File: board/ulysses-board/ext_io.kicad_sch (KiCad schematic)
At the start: 31 parts, among them J10 CAN_2, J6 AIN, J7 CAN_1, J8 DIO_1, J9 DIO_0, U12 25LCxxx, U13 MCP3204, U14 MCP2515-I/P, U15 MCP2562-E-P, U16 MCP2515-I/P, U17 MCP23S17, U18 MCP2562-E-P, Y1 16MHz, Y2 16MHz

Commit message: Make some minor fixes.
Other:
- note added: "Analog input"
- note removed: "ADC input"
- moved on the sheet: C19, U12

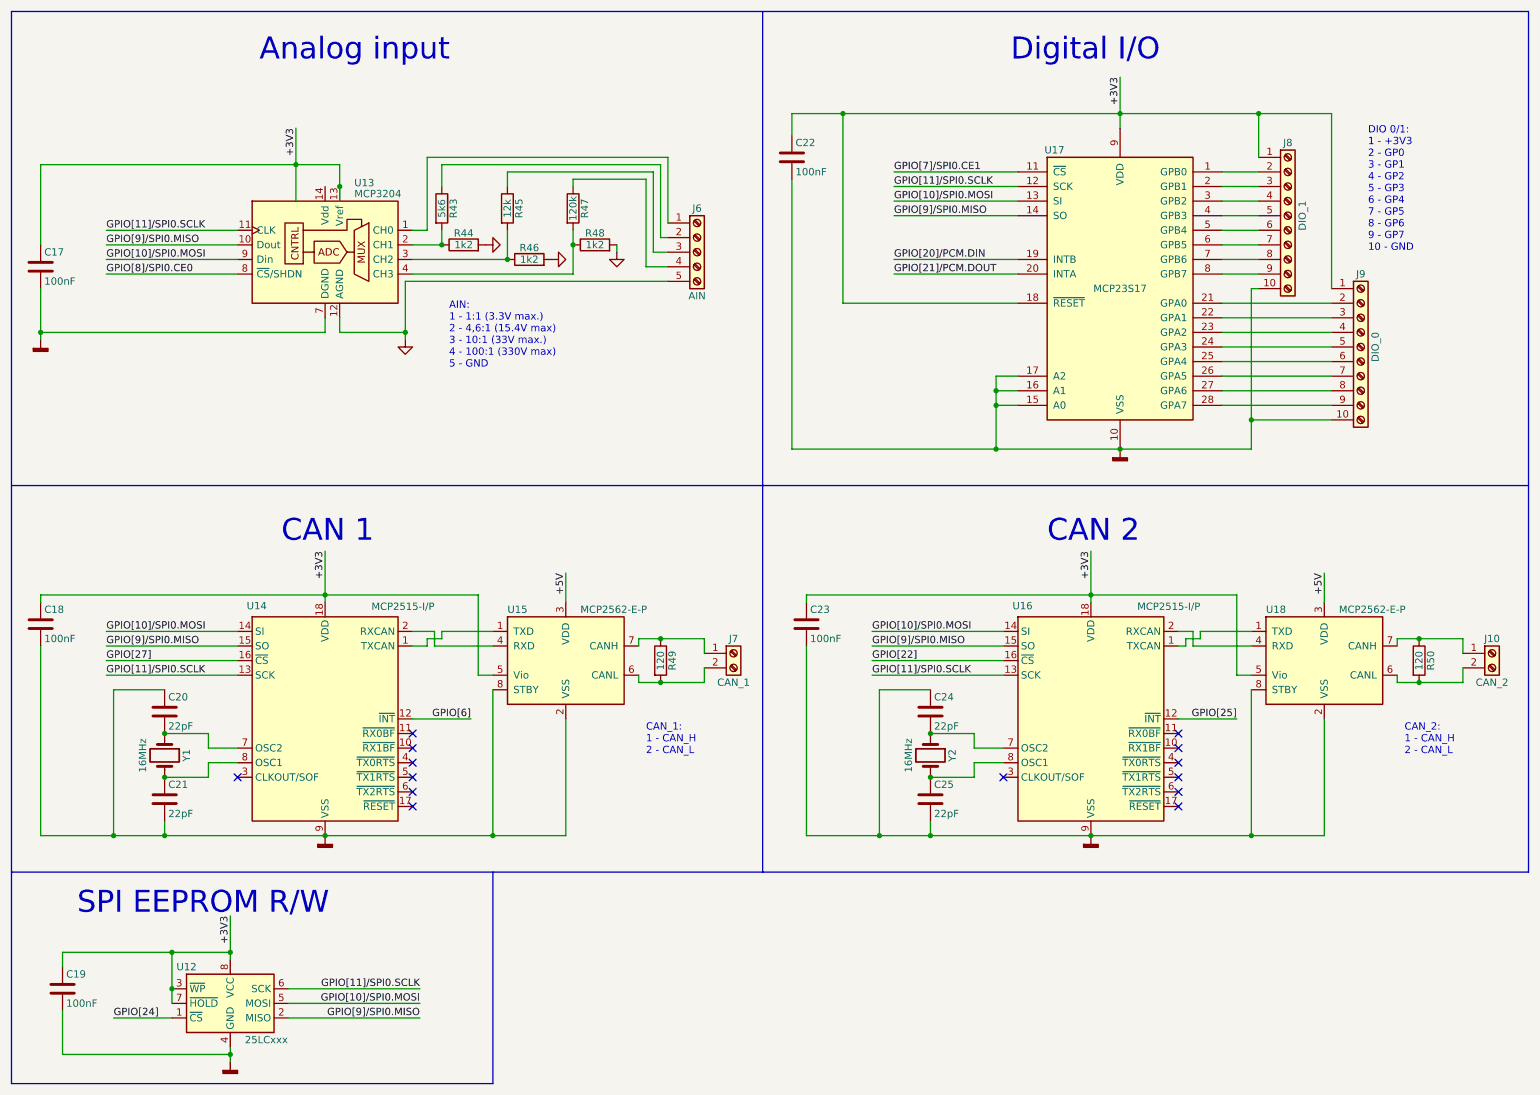
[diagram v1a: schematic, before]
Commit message: Add a real-time clock.
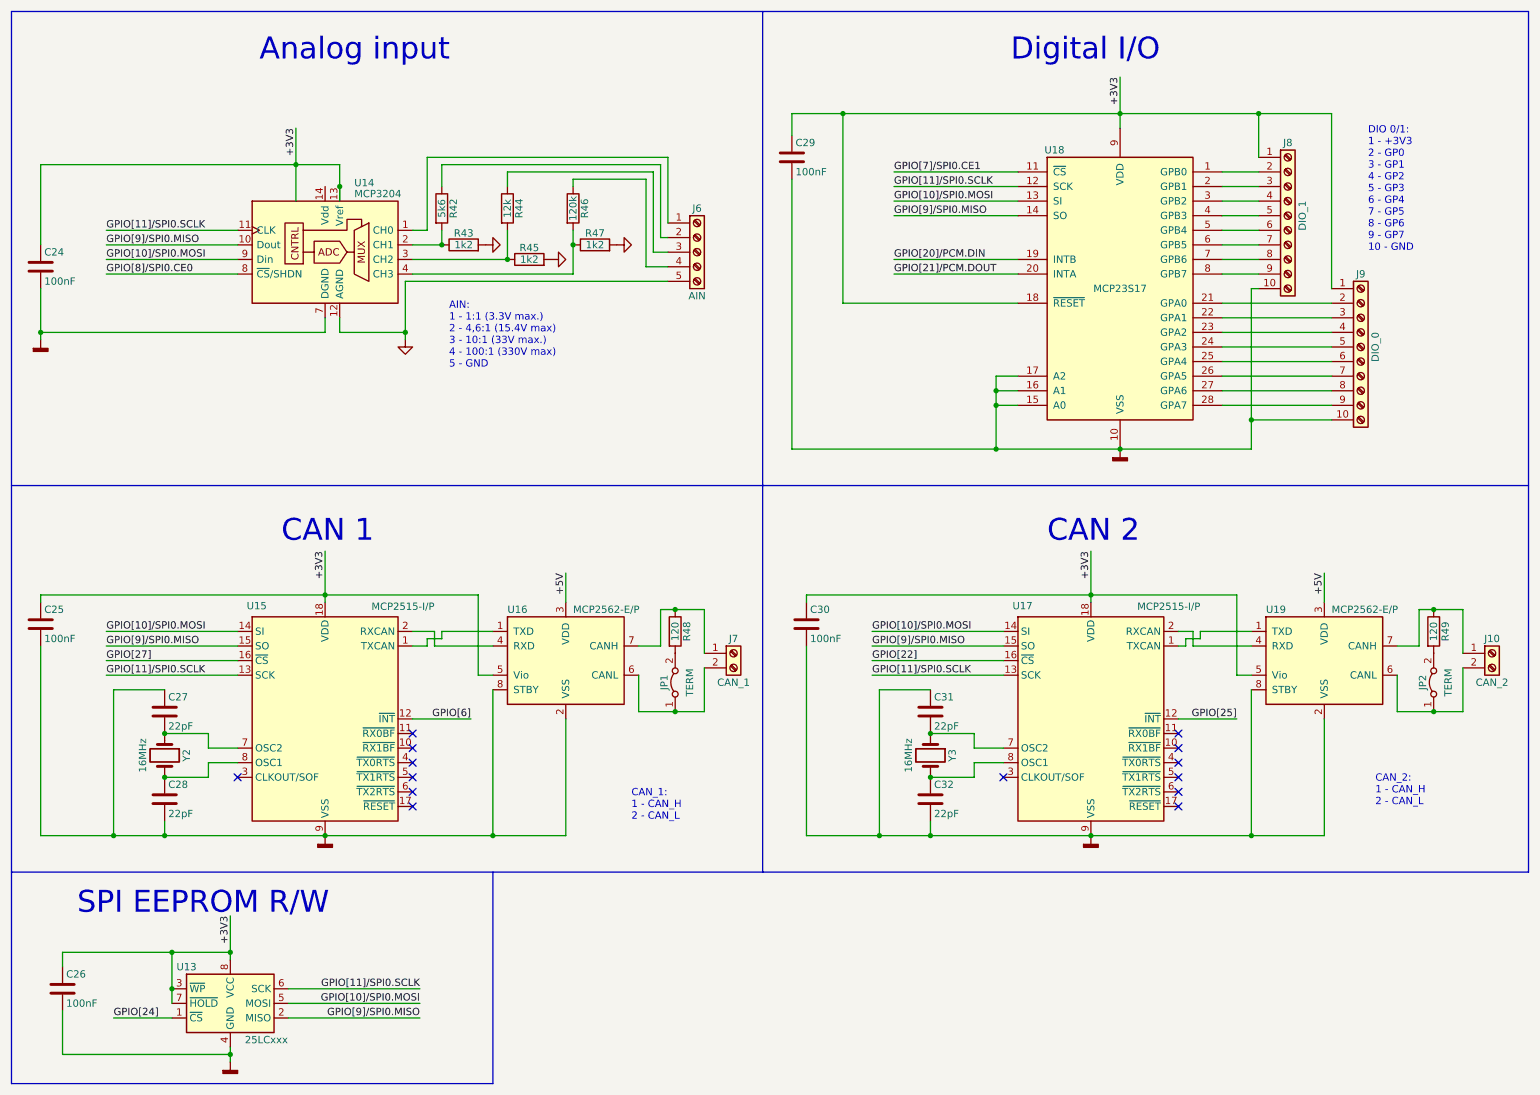
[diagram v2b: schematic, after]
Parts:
- added JP1: TERM, TestPoint:TestPoint_2Pads_Pitch2.54mm_Drill0.8mm, symbol Jumper:Jumper_2_Bridged
- added JP2: TERM, symbol Jumper:Jumper_2_Bridged
- U16: renamed from U15; value MCP2562-E-P -> MCP2562-E/P
- U19: renamed from U18; value MCP2562-E-P -> MCP2562-E/P
- renumbered C17 to C24, C18 to C25, C19 to C26, C20 to C27, C21 to C28, C22 to C29, C23 to C30, C24 to C31, C25 to C32, R43 to R42, R44 to R43, R45 to R44, R46 to R45, R47 to R46, R48 to R47, R49 to R48, R50 to R49, U12 to U13, U13 to U14, U14 to U15, U16 to U17, U17 to U18, Y1 to Y2, Y2 to Y3
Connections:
- net at J10.2 (Pin_2), U19.6 (CANL): now also JP2.1 (A); no longer R49.2
- net at J7.2 (Pin_2), U16.6 (CANL): now also JP1.1 (A); no longer R48.2
- new net: JP2.2 (B), R49.2
- new net: JP1.2 (B), R48.2
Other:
- moved on the sheet: R48, R49

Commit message: Make schemaics more readable.
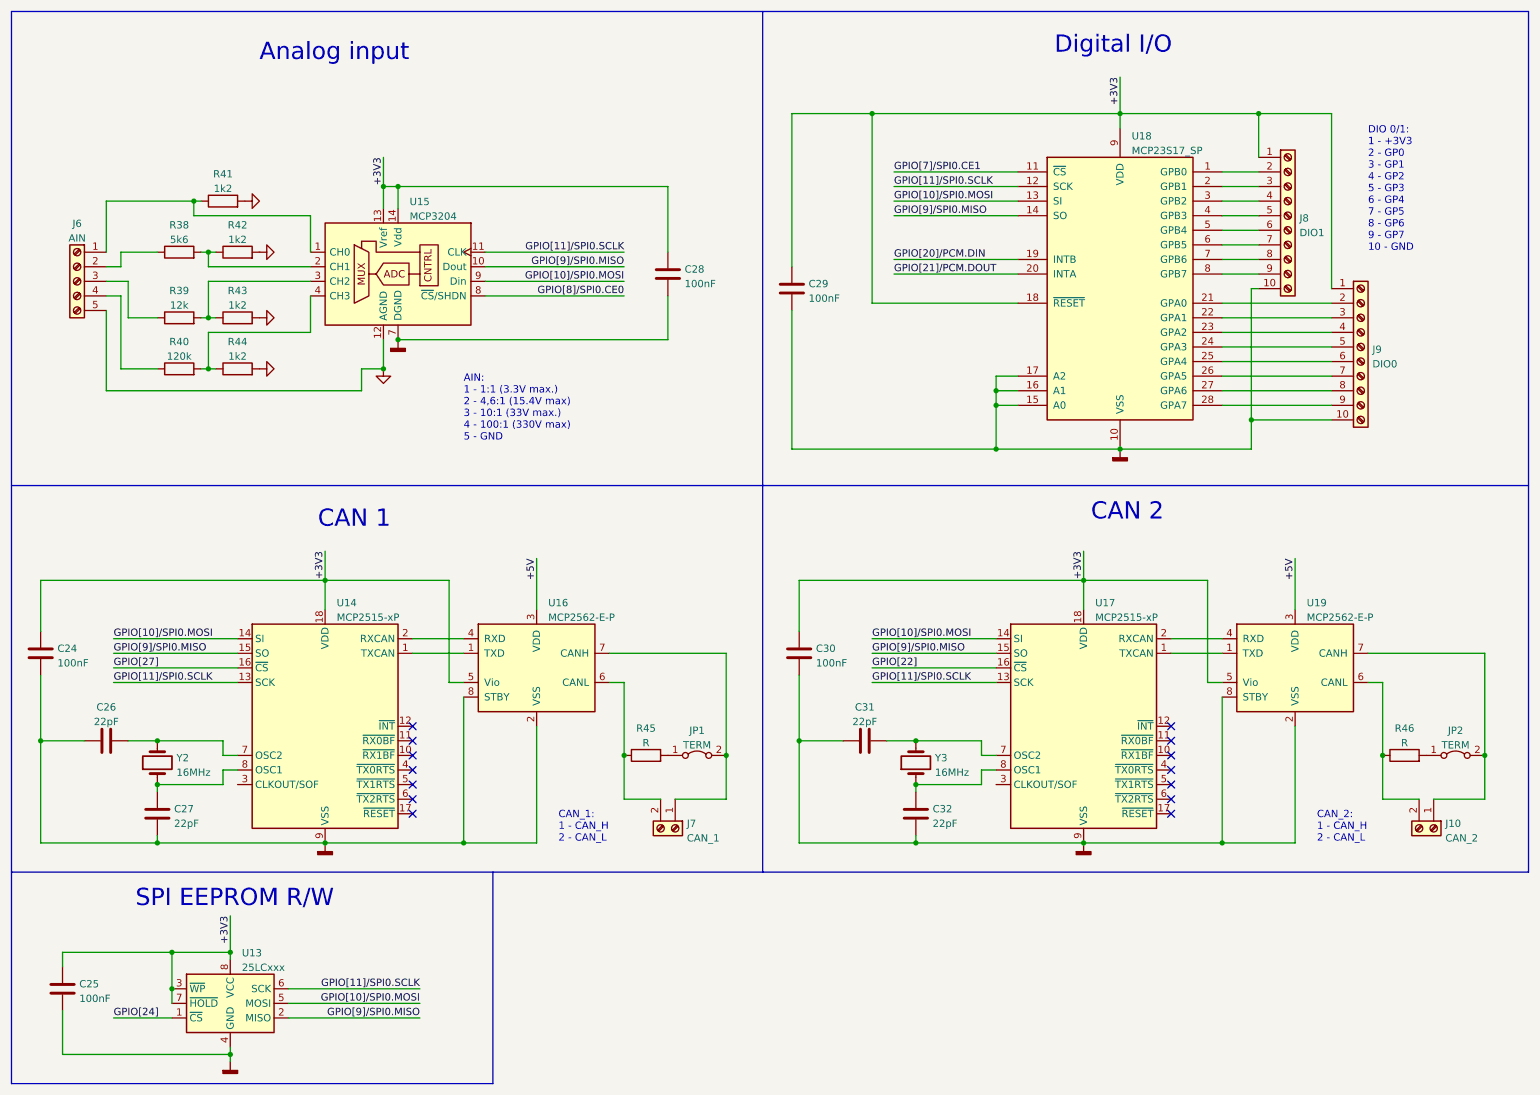
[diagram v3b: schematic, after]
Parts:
- removed R47: 1k2, symbol Device:R
- removed R48, R49: 120, symbol Device:R
- removed U14: MCP3204, symbol Analog_ADC:MCP3204
- removed U15, U17: MCP2515-I/P, Package_DIP:DIP-16_W7.62mm_LongPads, symbol Interface_CAN_LIN:MCP2515-xSO
- removed U16, U19: MCP2562-E/P, Package_DIP:DIP-8_W7.62mm, symbol Interface_CAN_LIN:MCP2562-E-P
- added R38: 5k6, symbol Device:R
- added R39: 12k, symbol Device:R
- added R40: 120k, symbol Device:R
- added R41: 1k2, symbol Device:R
- added U14, U17: MCP2515-xP, Package_DIP:DIP-18_W7.62mm_Socket_LongPads, symbol Interface_CAN_LIN_custom:MCP2515-xP
- added U15: MCP3204, symbol Analog_ADC:MCP3204
- added U16, U19: MCP2562-E-P, Package_DIP:DIP-8_W7.62mm, symbol Interface_CAN_LIN_custom:MCP2562-E-P
- C26: value 100nF -> 22pF
- C28: value 22pF -> 100nF
- J8: value DIO_1 -> DIO1
- J9: value DIO_0 -> DIO0
- JP1: footprint TestPoint:TestPoint_2Pads_Pitch2.54mm_Drill0.8mm -> (none)
- R42: value 5k6 -> 1k2
- R44: value 12k -> 1k2
- R45: value 1k2 -> R
- R46: value 120k -> R
- U18: value MCP23S17 -> MCP23S17_SP; footprint Package_DIP:DIP-28_W7.62mm_Socket_LongPads -> Package_DIP:DIP-28_W7.62mm
- Y2, Y3: footprint Crystal:Crystal_HC52-6mm_Vertical -> (none)
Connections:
- net +3V3: now also C24.2, C28.2, C30.2, U14.18 (VDD), U15.13 (Vref), U15.14 (Vdd), U16.5 (Vio), U17.18 (VDD), U19.5 (Vio); no longer C24.1, C26.1, C30.1
- net +5V: now also U16.3 (VDD), U19.3 (VDD)
- net GNDA: now also R42.2, R44.2, R41.2, U15.12 (AGND); no longer R45.2
- net GNDD: now also C24.1, C26.1, C27.2, C28.1, C30.1, U14.9 (VSS), U15.7 (DGND), U16.2 (VSS), U16.8 (STBY), U17.9 (VSS), U19.2 (VSS), U19.8 (STBY); no longer C24.2, C26.2, C27.1, C28.2, C30.2
- net GPIO[10]/SPI0.MOSI: now also U14.14 (SI), U15.9 (Din), U17.14 (SI)
- net GPIO[11]/SPI0.SCLK: now also U14.13 (SCK), U15.11 (CLK), U17.13 (SCK)
- net GPIO[22]: now also U17.16 (~{CS})
- net GPIO[27]: now also U14.16 (~{CS})
- net GPIO[8]/SPI0.CE0: now also U15.8 (~{CS}/SHDN)
- net GPIO[9]/SPI0.MISO: now also U14.15 (SO), U15.10 (Dout), U17.15 (SO)
- net at Y3.2: now also C31.2, U17.7 (OSC2); no longer C32.1
- net at J10.1 (Pin_1): now also JP2.2 (B), U19.7 (CANH)
- net at J7.1 (Pin_1): now also JP1.2 (B), U16.7 (CANH)
- net at J7.2 (Pin_2): now also R45.1, U16.6 (CANL); no longer JP1.1 (A)
- net at R44.1: now also R40.2, U15.4 (CH3); no longer J6.3 (Pin_3)
- net at Y2.2: now also C26.2, U14.7 (OSC2); no longer C28.1
- net at R46.2: now also JP2.1 (A)
- net at J6.1 (Pin_1): now also R41.1, U15.1 (CH0)
- net at R43.1: now also R39.2, U15.3 (CH2); no longer R42.2
- net at J10.2 (Pin_2): now also R46.1, U19.6 (CANL); no longer JP2.1 (A)
- net at J6.4 (Pin_4): now also R40.1; no longer R46.1
- net at Y3.1: now also C32.1, U17.8 (OSC1); no longer C31.2
- net at R42.1: now also R38.2, U15.2 (CH1); no longer J6.2 (Pin_2)
- net at Y2.1: now also C27.1, U14.8 (OSC1); no longer C27.2
- new net: J6.2 (Pin_2), R38.1
- new net: J6.3 (Pin_3), R39.1
- new net: U14.1 (TXCAN), U16.1 (TXD)
- new net: U14.2 (RXCAN), U16.4 (RXD)
- new net: JP1.1 (A), R45.2
- new net: U17.1 (TXCAN), U19.1 (TXD)
- new net: U17.2 (RXCAN), U19.4 (RXD)

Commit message: Some minor imptovements.
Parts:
- removed JP1, JP2: TERM, symbol Jumper:Jumper_2_Bridged
- added SW? (x2): Term, symbol Switch:SW_DIP_x01
- R45, R46: value R -> 120
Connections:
- net at R46.2: now also SW?.1
- net at J10.1 (Pin_1), U19.7 (CANH): now also SW?.2
- net at J7.1 (Pin_1): now also SW?.2; no longer U16.7 (CANH)
- net at R45.2: now also SW?.1
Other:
- moved on the sheet: C25, C28, J10, J6, J7, R38, R39, R40, R41, R42, R43, R44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
